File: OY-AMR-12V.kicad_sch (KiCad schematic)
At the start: 26 parts

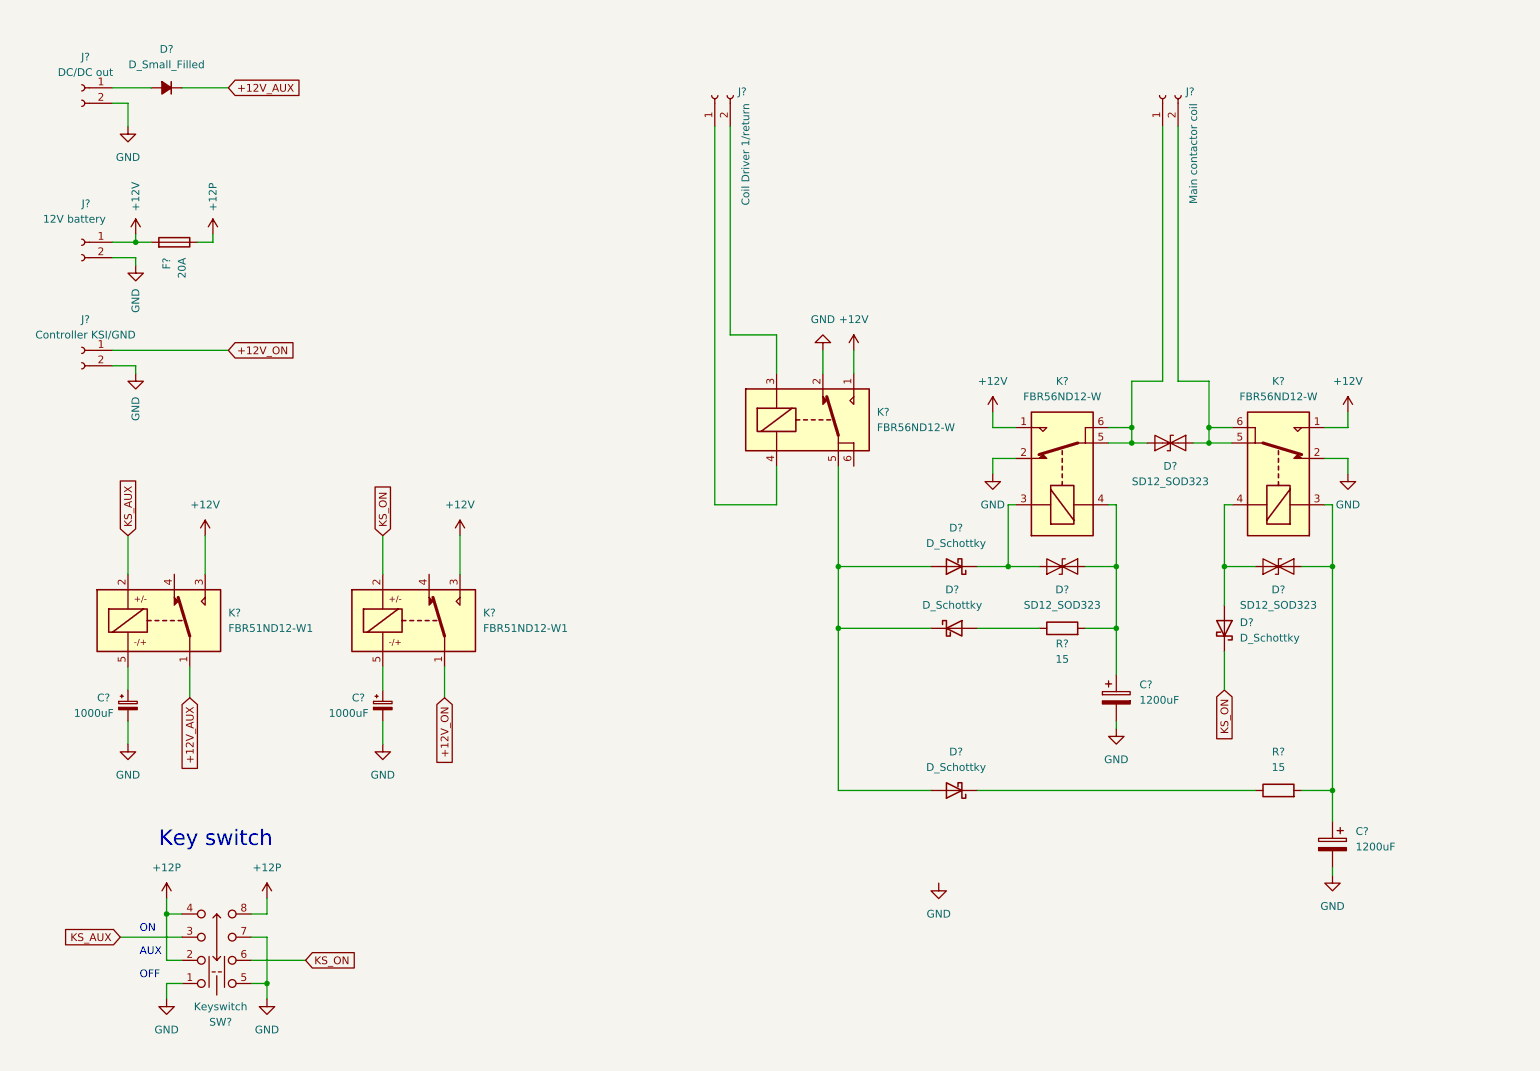
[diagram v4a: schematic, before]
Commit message: Simplified & changed to available components
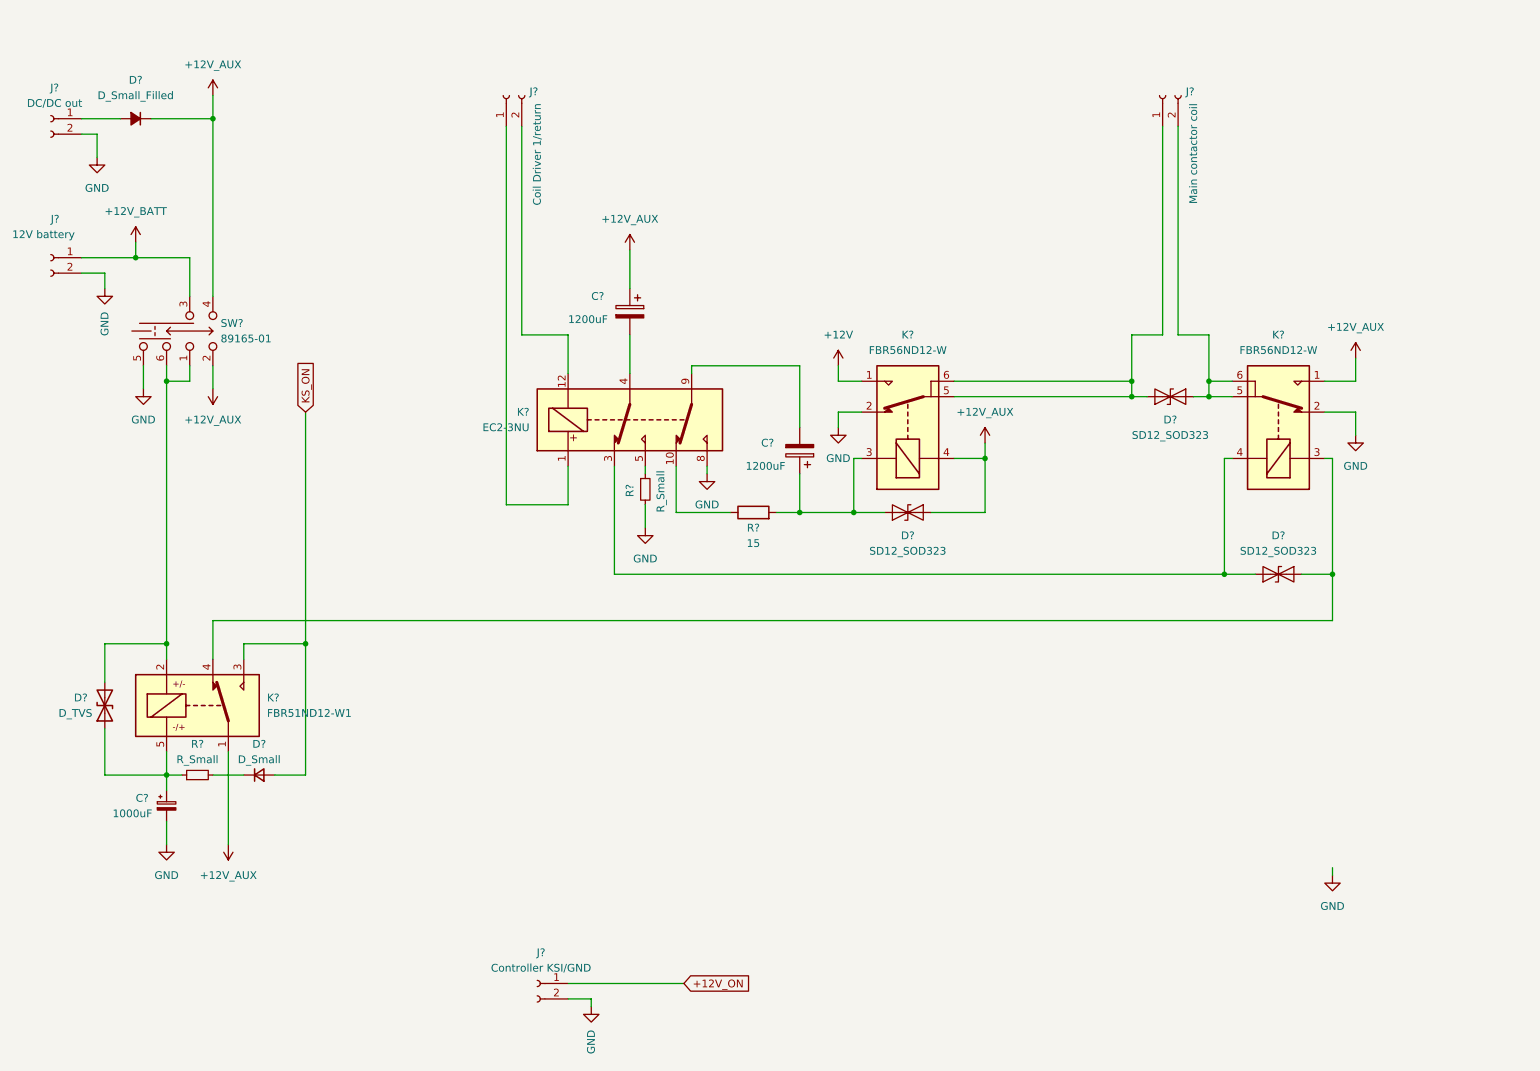
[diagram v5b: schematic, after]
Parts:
- removed C?: 1000uF, symbol Device:C_Polarized_Small
- removed D? (x4): D_Schottky, symbol Device:D_Schottky
- removed F?: 20A, symbol Device:Fuse
- removed K?: FBR56ND12-W, Relay_THT:Relay_SPDT_Omron_G6E, symbol Miscellaneous:FBR56ND12-W
- removed K?: FBR51ND12-W1, Relay_THT:Relay_SPDT_Omron_G6E, symbol Miscellaneous:FBR51ND12-W1
- removed R?: 15, symbol Device:R
- removed SW?: Keyswitch, symbol Miscellaneous:H200AA2F205NQ
- added D?: D_Small, symbol Device:D_Small
- added D?: D_TVS, symbol Device:D_TVS
- added K?: EC2-3NU, Relay_THT:Relay_DPDT_Kemet_EC2, symbol Relay:EC2-3NU
- added R? (x2): R_Small, symbol Device:R_Small
- added SW?: 89165-01, symbol Miscellaneous:89165-01
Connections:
- net +12V: no longer J?.1 (Pin_1), K?.1, K?.3
- net +12V_AUX: now also C?.1, D?.2 (A2), K?.1, K?.1, K?.4, SW?.2 (B), SW?.4 (D)
- net +12V_ON: no longer K?.1
- net GND: now also K?.8, R?.2, SW?.5 (E); no longer C?.2, C?.2
- net KS_ON: now also K?.3, D?.2 (A); no longer K?.2
- net at J?.1 (Pin_1): now also K?.1
- net at J?.2 (Pin_2): now also K?.12
- net at D?.2 (A2), K?.3: now also K?.4; no longer C?.1
- net at C?.1, R?.2: now also D?.1 (A1), K?.3; no longer D?.2 (A2), K?.4
- net at R?.1: now also K?.10
- net at D?.1 (A1), K?.4: now also K?.3
- net at C?.1, K?.5: now also D?.1 (A1), R?.1
- new net: C?.2, K?.4
- new net: D?.2 (A2), K?.2, SW?.1 (A), SW?.6 (F)
- new net: C?.2, K?.9
- new net: D?.1 (K), R?.2
- new net: K?.5, R?.1
- new net +12V_BATT: J?.1 (Pin_1), SW?.3 (C)
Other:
- note removed: "AUX"
- note removed: "Key switch"
- note removed: "OFF"
- note removed: "ON"
- moved on the sheet: C?, D?, J?, K?, R?

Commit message: Reduced schematics to PCB contents
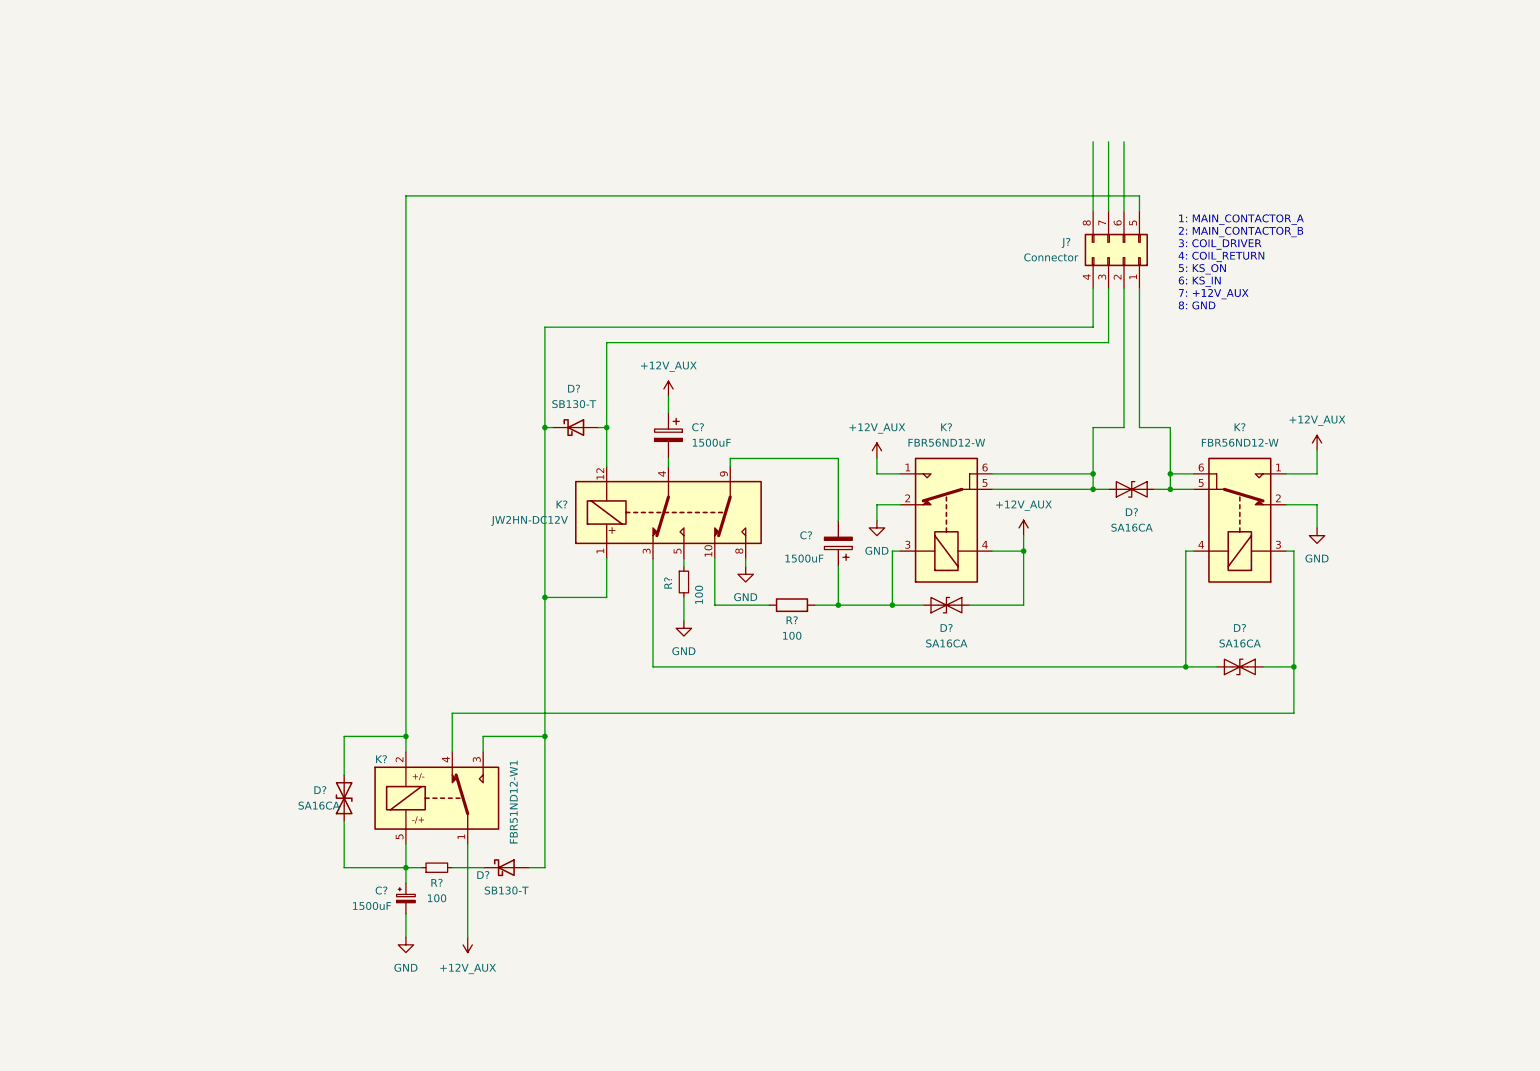
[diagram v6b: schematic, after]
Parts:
- removed D?: D_Small, symbol Device:D_Small
- removed D?: D_Small_Filled, symbol Device:D_Small_Filled
- removed J?: Coil Driver 1/return, symbol Connector:Conn_01x02_Female
- removed J?: 12V battery, symbol Connector:Conn_01x02_Female
- removed J?: Controller KSI/GND, symbol Connector:Conn_01x02_Female
- removed J?: DC/DC out, symbol Connector:Conn_01x02_Female
- removed J?: Main contactor coil, symbol Connector:Conn_01x02_Female
- removed SW?: 89165-01, symbol Miscellaneous:89165-01
- added D? (x2): SB130-T, symbol Device:D_Schottky
- added J?: Connector, symbol Connector_Generic:Conn_02x04_Top_Bottom
- C? (x2): value 1200uF -> 1500uF
- C?: value 1000uF -> 1500uF
- D? (x3): value SD12_SOD323 -> SA16CA
- D?: value D_TVS -> SA16CA
- K?: value EC2-3NU -> JW2HN-DC12V
- R? (x2): value R_Small -> 100
- R?: value 15 -> 100
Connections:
- net +12V is gone; now on net +12V_AUX: K?.1
- net KS_ON is gone; now on an unnamed net: K?.3
- net at K?.1: now also D?.1 (K), D?.2 (A), J?.4 (Pin_4)
- net at K?.12: now also D?.2 (A), J?.3 (Pin_3)
- net at D?.2 (A2), K?.2: now also J?.5 (Pin_5)
- net at R?.2: now also D?.1 (K)
- net at D?.2 (A2), K?.5, K?.6: now also J?.1 (Pin_1)
- net at D?.1 (A1), K?.5, K?.6: now also J?.2 (Pin_2)
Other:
- note added: "1: MAIN_CONTACTOR_A 2: MAIN_CONTACTOR_B 3: COIL_DRIVER 4: COIL_RETURN 5: KS_ON 6: KS_IN 7: +12V_AUX 8: GND"
- moved on the sheet: C?, D?, K?, R?

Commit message: Added charging diode, connectors, revise latching relay type
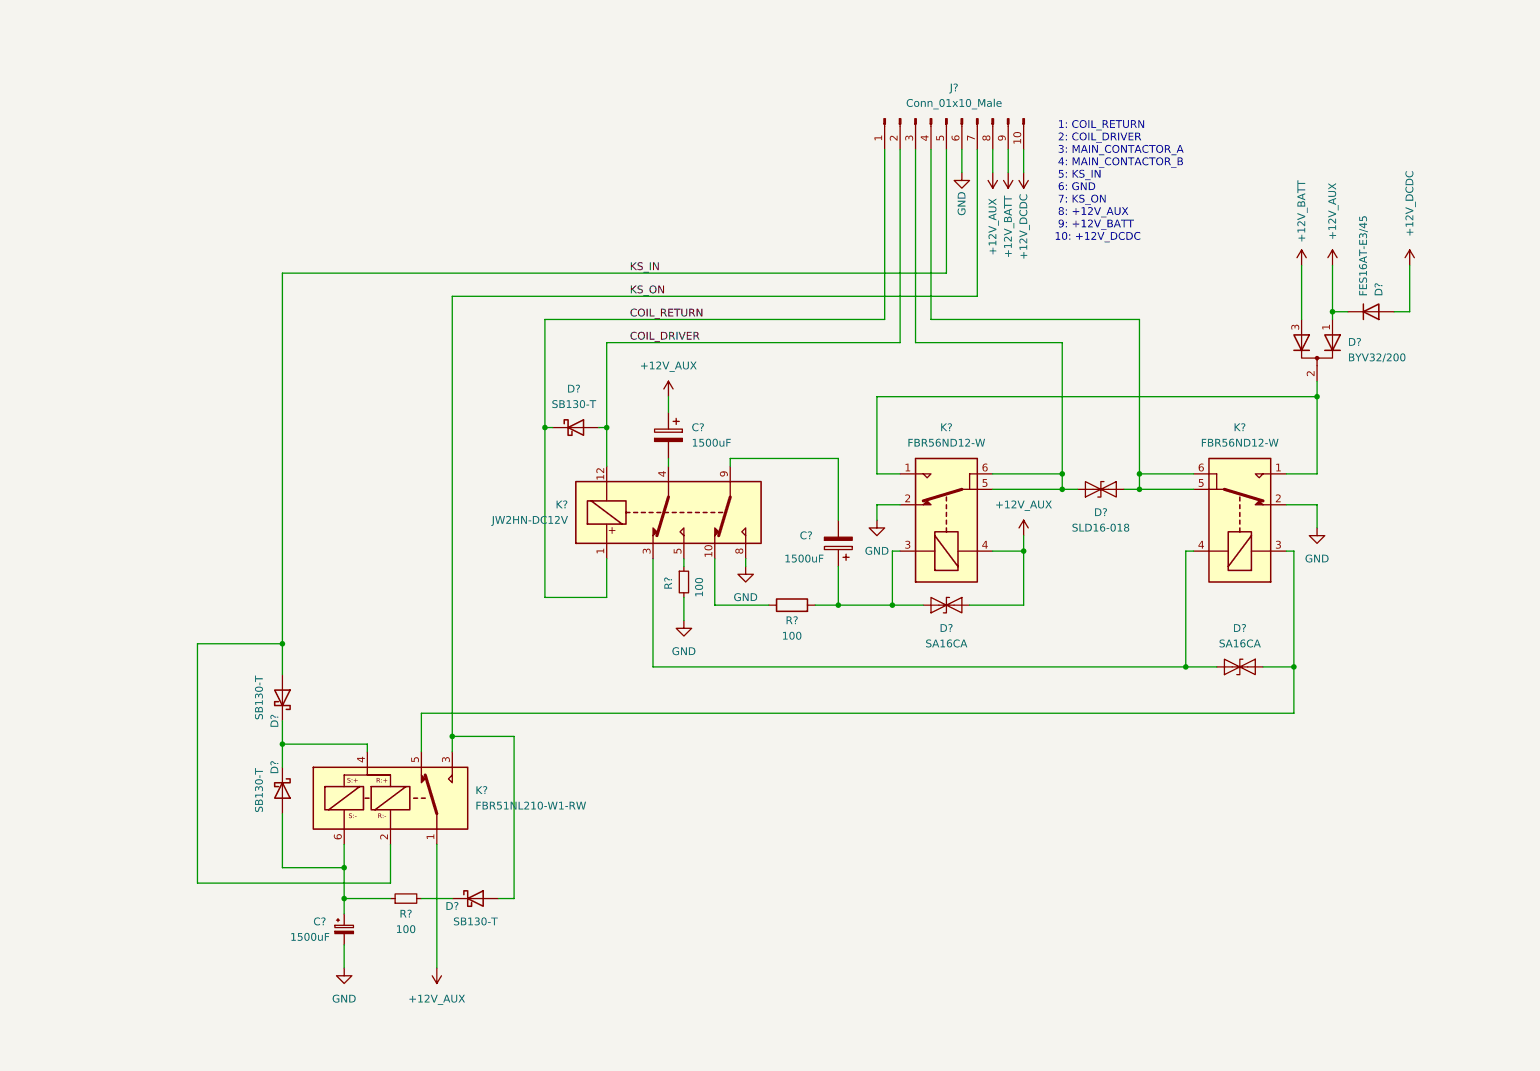
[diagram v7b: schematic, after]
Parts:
- removed D?: SA16CA, symbol Device:D_TVS
- removed J?: Connector, symbol Connector_Generic:Conn_02x04_Top_Bottom
- removed K?: FBR51ND12-W1, Relay_THT:Relay_SPDT_Omron_G6E, symbol Miscellaneous:FBR51ND12-W1
- added D?: FES16AT-E3/45, symbol Device:D
- added D? (x2): SB130-T, symbol Device:D_Schottky
- added D?: BYV32/200, symbol Device:D_Dual_CommonCathode_AKA_Parallel
- added J?: Conn_01x10_Male, symbol Connector:Conn_01x10_Male
- added K?: FBR51NL210-W1-RW, symbol Miscellaneous:FBR51NL210-W1-RW
- D?: value SA16CA -> SLD16-018; footprint Diode_SMD:D_SOD-323 -> (none)
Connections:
- net +12V_AUX: now also D?.1 (K), D?.1 (K), J?.8 (Pin_8), K?.1; no longer K?.1, K?.1
- net GND: now also J?.6 (Pin_6)
- net at C?.1, R?.1: now also D?.2 (A), K?.6
- net at D?.2 (A2), K?.5, K?.6: now also J?.4 (Pin_4)
- net at D?.1 (A1), K?.5, K?.6: now also J?.3 (Pin_3)
- net COIL_DRIVER: now reaches D?.2 (A), K?.12
- net COIL_DRIVER: now also J?.2 (Pin_2)
- net COIL_RETURN: now reaches D?.1 (K), K?.1
- net COIL_RETURN: now also J?.1 (Pin_1); no longer D?.2 (A)
- net at D?.2 (A2), K?.3: now also K?.5
- new net: D?.1 (K), D?.1 (K), K?.4
- new net: D?.2 (A), K?.1, K?.1
- new net +12V_BATT: D?.3 (K), J?.9 (Pin_9)
- new net +12V_DCDC: D?.2 (A), J?.10 (Pin_10)
- new net KS_IN: D?.2 (A), J?.5 (Pin_5), K?.2
- new net KS_ON: D?.2 (A), J?.7 (Pin_7), K?.3
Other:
- note added: "1: COIL_RETURN 2: COIL_DRIVER 3: MAIN_CONTACTOR_A 4: MAIN_CONTACTOR_B 5: KS_IN 6: GND 7: KS_ON 8: +12V_AUX 9: +12V_BATT 10: +12V_DCDC"
- note removed: "1: MAIN_CONTACTOR_A 2: MAIN_CONTACTOR_B 3: COIL_DRIVER 4: COIL_RETURN 5: KS_ON 6: KS_IN 7: +12V_AUX 8: GND"
- moved on the sheet: C?, D?, R?
